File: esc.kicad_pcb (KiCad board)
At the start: 4 copper layers, 68.3 x 63.8 mm, 73 parts, among them J1 Conn_01x02, J2 Screw_Terminal_01x01, J3 Screw_Terminal_01x01, J4 Screw_Terminal_01x01, J5 3220-10-0100-00, Q1 SIR182DP-T1-RE3, Q2 SIR182DP-T1-RE3, Q3 SIR182DP-T1-RE3, Q4 SIR182DP-T1-RE3, Q5 SIR182DP-T1-RE3, Q6 SIR182DP-T1-RE3, SW1 RotaryEncoder, U1 TPS7A20xxxDQN, U2 STM32G484CETx, U3 TPS562201DDCR, U4 TVS0500DRV, U5 IR2103STRPBF, U6 IR2103STRPBF, U7 IR2103STRPBF, Y1 32.768KHz

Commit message: cleaning routing
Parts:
- moved C25 1.56 mm to (131.4, 93.2)
- moved C2 1.56 mm to (131.4, 89.8)
- moved C20 1.56 mm to (131.4, 91.5)
- moved C30 1.56 mm to (131.4, 94.8)
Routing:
- net /STM32/W_HIN: track 2.13 -> 41.8 mm, vias 0 -> 2
- net /STM32/U_LIN: track 0.00 -> 21.8 mm, vias 0 -> 2
- net /STM32/U_HIN: track 0.00 -> 20.9 mm, vias 0 -> 2
- net /STM32/V_HIN: track 1.76 -> 15.9 mm, vias 0 -> 2
- net VCC: track 13.0 -> 23.6 mm
- net /STM32/V_LIN: track 8.57 -> 15.6 mm, vias 0 -> 2
- net GND: track 75.8 -> 76.7 mm, vias 46 -> 49
- net /STM32/W_LIN: track 27.8 -> 27.9 mm, vias 0 -> 2

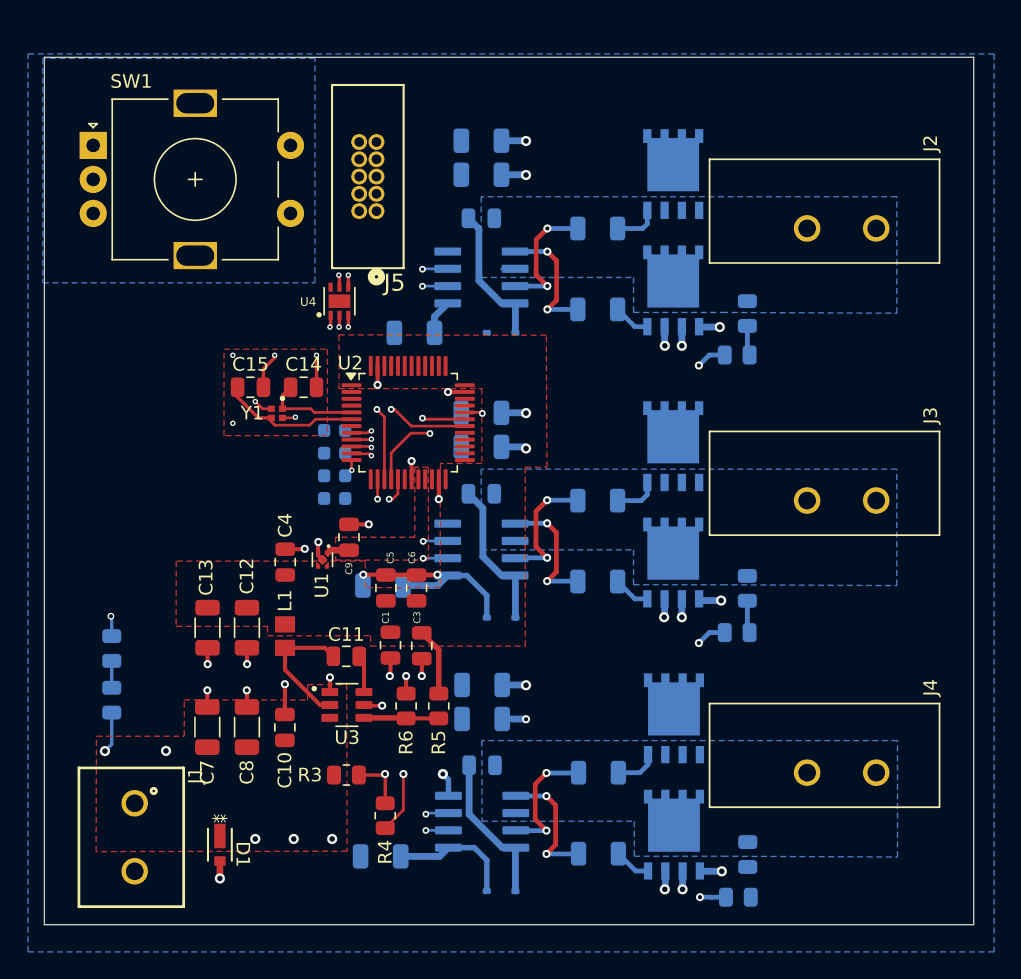
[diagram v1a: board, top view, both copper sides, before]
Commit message: cleaning sensing routing
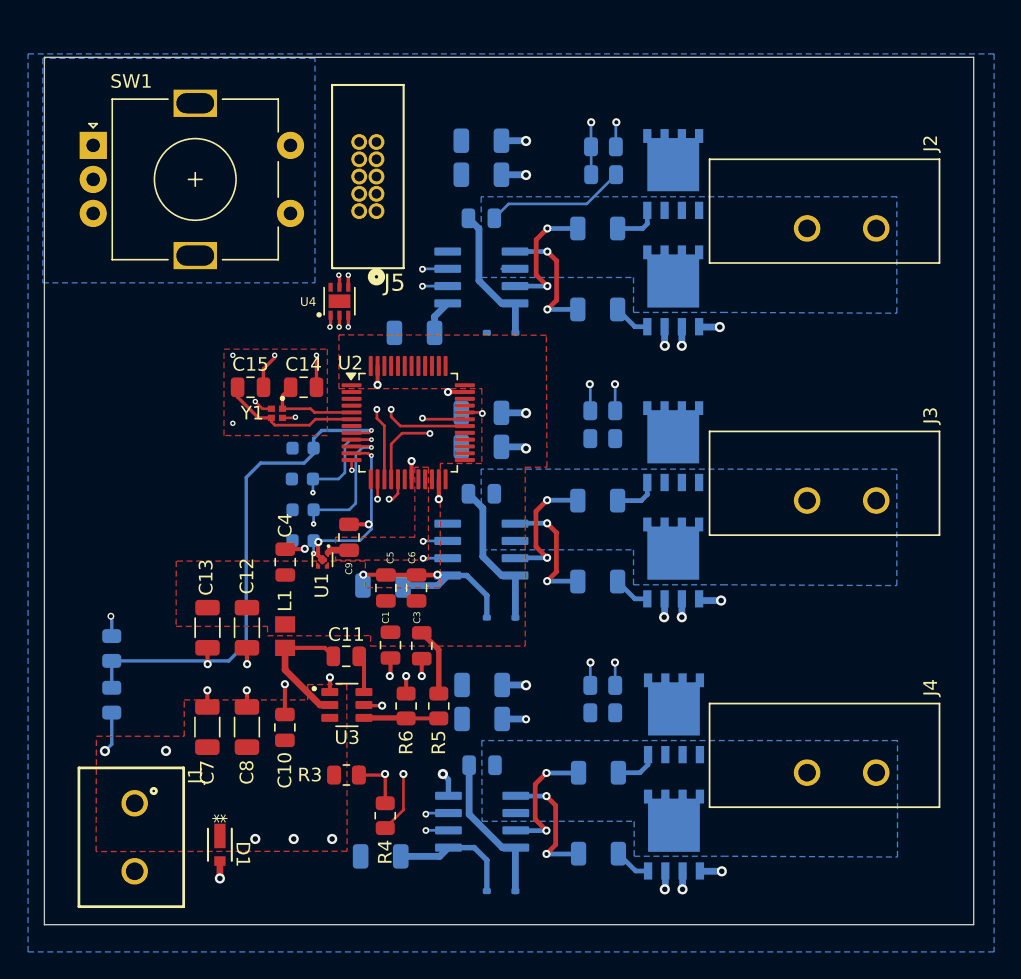
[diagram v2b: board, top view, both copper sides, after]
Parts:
- moved R14 19.1 mm to (151.2, 88.4), turned to 0 degrees
- moved R18 18.5 mm to (151.2, 108.6), turned to 0 degrees
- moved R10 18.2 mm to (151.2, 69.0), turned to 0 degrees
- moved R13 15.3 mm to (151.2, 90.5), turned to 180 degrees
- moved R17 14.9 mm to (151.2, 110.6), turned to 180 degrees
- moved R9 14.7 mm to (151.2, 71.0), turned to 180 degrees
- moved C30 3.87 mm to (129.1, 98.0)
- moved C25 3.41 mm to (129.1, 95.7)
- moved C20 3.04 mm to (129.1, 93.4)
- moved C2 2.66 mm to (129.1, 91.2)
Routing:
- net /STM32/W_VSENSE: track 1.52 -> 70.9 mm, vias 1 -> 3
- net /STM32/V_VSENSE: track 3.88 -> 62.3 mm, vias 1 -> 3
- net /STM32/U_VSENSE: track 3.69 -> 60.3 mm, vias 1 -> 3
- net /PWR/VCC_SENSE: track 3.50 -> 37.4 mm
- net /U PHASE/U_PHASE: track 0.98 -> 11.3 mm
- net GND: track 76.7 -> 75.8 mm

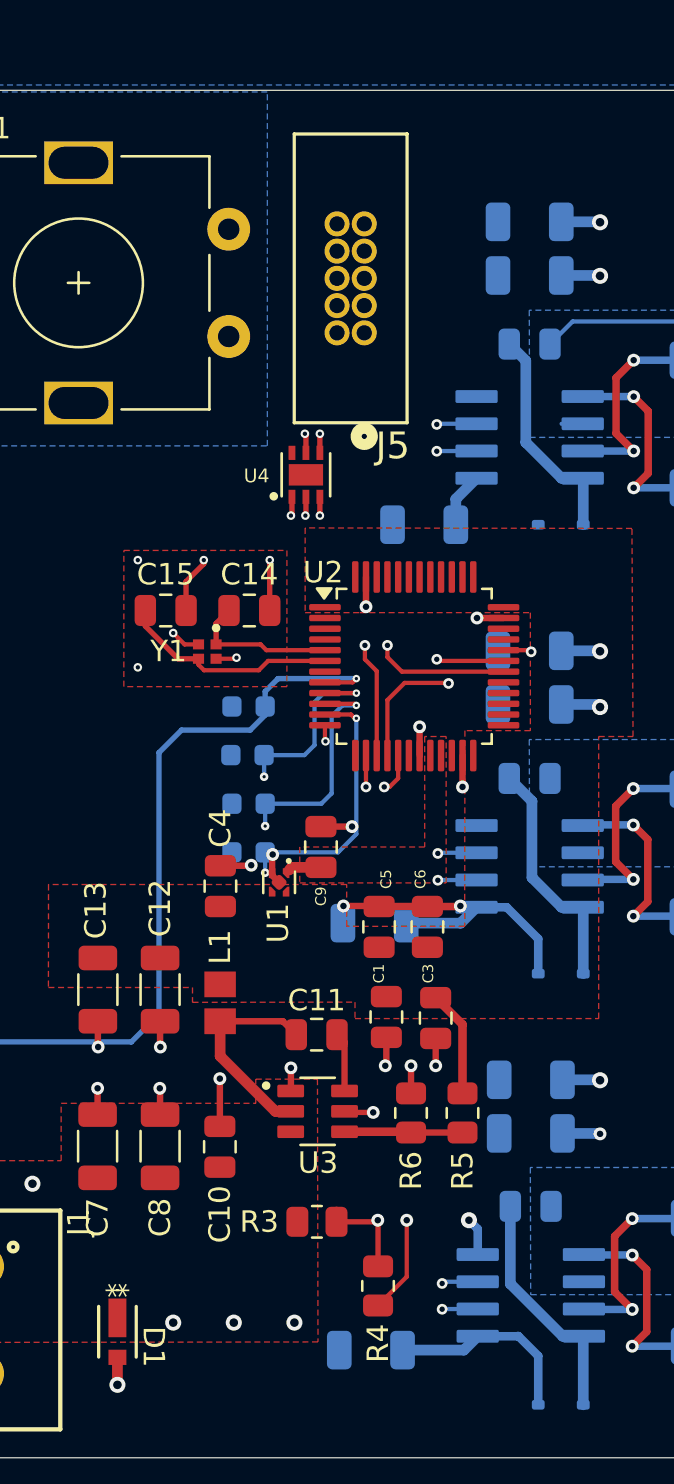
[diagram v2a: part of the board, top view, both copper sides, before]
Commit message: SWD TVS routing
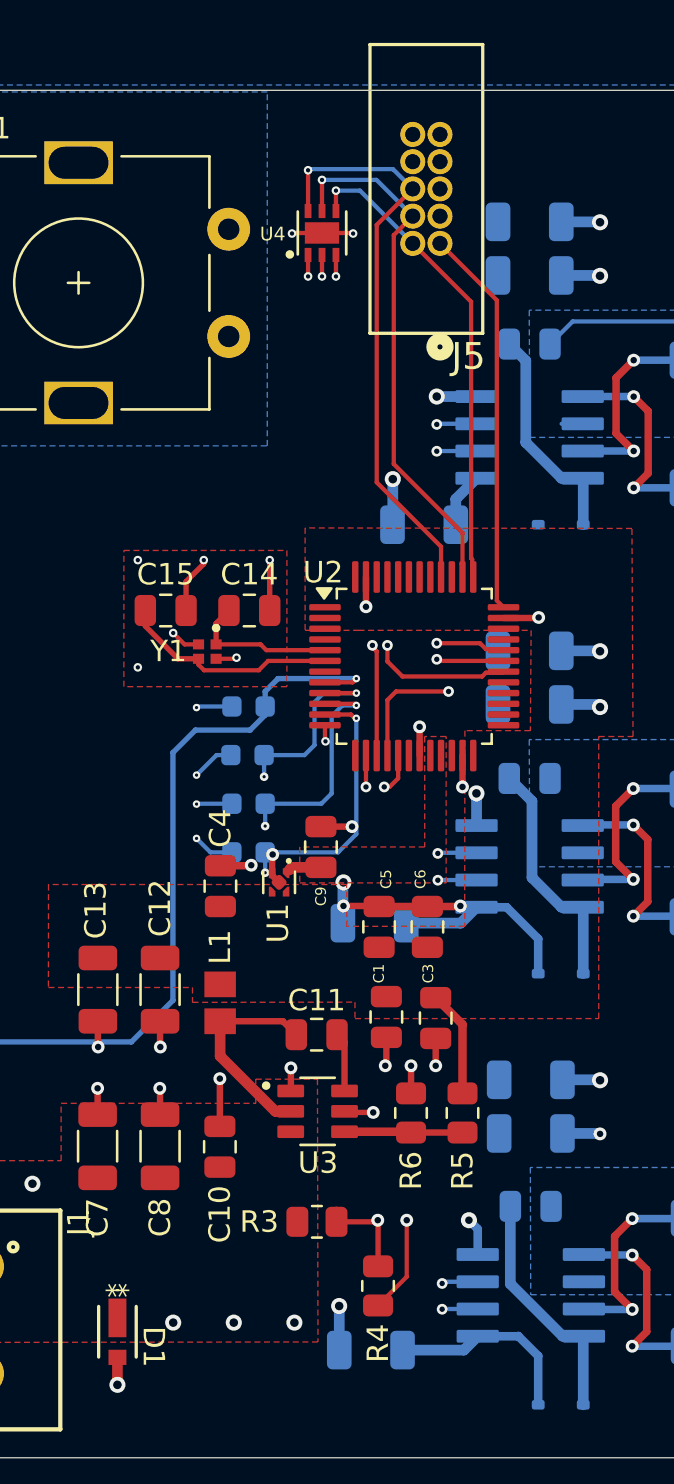
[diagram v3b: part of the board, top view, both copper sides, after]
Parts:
- moved U4 11.3 mm to (132.6, 69.1)
- moved J5 5.46 mm to (138.1, 69.6)
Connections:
- U4 pad 7: (no net) -> GND
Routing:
- net /STM32/SWO: track 0.00 -> 27.3 mm, vias 0 -> 1
- net /STM32/SWCLK: track 1.52 -> 25.0 mm
- net /STM32/SWDIO: track 0.92 -> 22.3 mm
- net GND: track 75.8 -> 96.1 mm, vias 49 -> 60
- net +3V3: track 4.98 -> 23.2 mm
- net /STM32/ENC_A: track 45.8 -> 41.3 mm
- net /STM32/U_VSENSE: track 60.3 -> 56.0 mm
- net /STM32/W_HIN: track 41.8 -> 39.1 mm
- net /STM32/ENC_B: track 42.9 -> 40.3 mm
- net /STM32/W_VSENSE: track 70.9 -> 72.0 mm
- net /STM32/V_LIN: track 16.0 -> 15.4 mm

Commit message: DRC cleanup
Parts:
- moved U4 6.90 mm to (132.6, 76.0)
- moved J5 4.50 mm to (138.1, 74.1)
- moved J1 1.00 mm to (115.8, 119.8)
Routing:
- net /V PHASE/V_PHASE: track 0.00 -> 11.4 mm
- net /W PHASE/W_PHASE: track 0.00 -> 11.0 mm
- net /STM32/SWDIO: track 22.3 -> 16.5 mm
- net /STM32/SWCLK: track 25.0 -> 20.2 mm
- net +3V3: track 23.2 -> 18.7 mm
- net VCC: track 23.6 -> 27.8 mm
- net /STM32/SWO: track 27.3 -> 23.3 mm
- net /STM32/V_VSENSE: track 62.3 -> 64.4 mm
- net /STM32/W_VSENSE: track 72.0 -> 74.1 mm
- net /STM32/U_VSENSE: track 56.0 -> 57.9 mm

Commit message: DRC cleanup
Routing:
- net GND: track 96.1 -> 97.7 mm
- net VCC: track 27.8 -> 26.8 mm
